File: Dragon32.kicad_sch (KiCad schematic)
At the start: 7 parts, among them IC14 74LS86AN, IC22 74LS00N, IC23 74ALS74N, IC25 LM393P, IC28 74LS393N, IC31 74LS02N

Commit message: repack layout
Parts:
- added JP4: 5vPower, Connector_PinHeader_2.54mm:PinHeader_1x02_P2.54mm_Vertical, symbol Connector:Conn_01x02_Pin
- added PL8: EDAC 392-040-558-201, Connector_PinHeader_2.54mm:PinHeader_2x20_P2.54mm_Vertical, symbol Connector_Generic:Conn_01x40
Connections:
- net +12V: now also PL8.1 (Pin_1), PL8.2 (Pin_2)
- net +5V: now also JP4.1 (Pin_1), PL8.9 (Pin_9)
- net A0: now also PL8.19 (Pin_19)
- net A1: now also PL8.20 (Pin_20)
- net A10: now also PL8.29 (Pin_29)
- net A11: now also PL8.30 (Pin_30)
- net A12: now also PL8.31 (Pin_31)
- net A13: now also PL8.37 (Pin_37)
- net A14: now also PL8.38 (Pin_38)
- net A15: now also PL8.39 (Pin_39)
- net A2: now also PL8.21 (Pin_21)
- net A3: now also PL8.22 (Pin_22)
- net A4: now also PL8.23 (Pin_23)
- net A5: now also PL8.24 (Pin_24)
- net A6: now also PL8.25 (Pin_25)
- net A7: now also PL8.26 (Pin_26)
- net A8: now also PL8.27 (Pin_27)
- net A9: now also PL8.28 (Pin_28)
- net CART: now also PL8.8 (Pin_8)
- net D0: now also PL8.10 (Pin_10)
- net D1: now also PL8.11 (Pin_11)
- net D2: now also PL8.12 (Pin_12)
- net D3: now also PL8.13 (Pin_13)
- net D4: now also PL8.14 (Pin_14)
- net D5: now also PL8.15 (Pin_15)
- net D6: now also PL8.16 (Pin_16)
- net D7: now also PL8.17 (Pin_17)
- net E: now also PL8.6 (Pin_6)
- net ESND: now also PL8.35 (Pin_35)
- net EXTMEN: now also PL8.40 (Pin_40)
- net GND: now also JP4.2 (Pin_2), PL8.33 (Pin_33), PL8.34 (Pin_34)
- net P2: now also PL8.36 (Pin_36)
- net Q: now also PL8.7 (Pin_7)
- net R2: now also PL8.32 (Pin_32)
- net R/~{W}: now also PL8.18 (Pin_18)
- net ~{HALT}: now also PL8.3 (Pin_3)
- net ~{NMI}: now also PL8.4 (Pin_4)
- net ~{RES}: now also PL8.5 (Pin_5)

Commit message: remove video
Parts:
- removed IC14: 74LS86AN, Package_DIP:DIP-14_W7.62mm, symbol 74xx:74LS86
- removed IC22: 74LS00N, Package_DIP:DIP-14_W7.62mm, symbol 74xx:74LS00
- removed IC23: 74ALS74N, Package_DIP:DIP-14_W7.62mm, symbol 74xx:74LS74
- removed IC28: 74LS393N, Package_DIP:DIP-14_W7.62mm, symbol 74xx:74LS393
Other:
- removed sheet VDG

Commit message: reinforce power rails
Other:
- added sheet Audio (audio.kicad_sch)
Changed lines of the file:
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@@
+    )
+  )
+  (sheet (at 266.7 210.82) (size 26.67 17.78) (fields_autoplaced)
+    (stroke (width 0.1524) (type solid))
+    (fill (color 0 0 0 0.0000))
+    (property "Sheetname" "Audio" (at 266.7 210.1084 0)
+      (effects (font (size 1.27 1.27)) (justify left bottom))
+    )
+    (property "Sheetfile" "audio.kicad_sch" (at 266.7 229.1846 0)
+      (effects (font (size 1.27 1.27)) (justify left top))
+    )
+    (instances
+      (project "Dragon32"
+        (path "/0c3dceba-7c95-4b3d-b590-0eb581444beb" (page "8"))
+      )
     )
   )

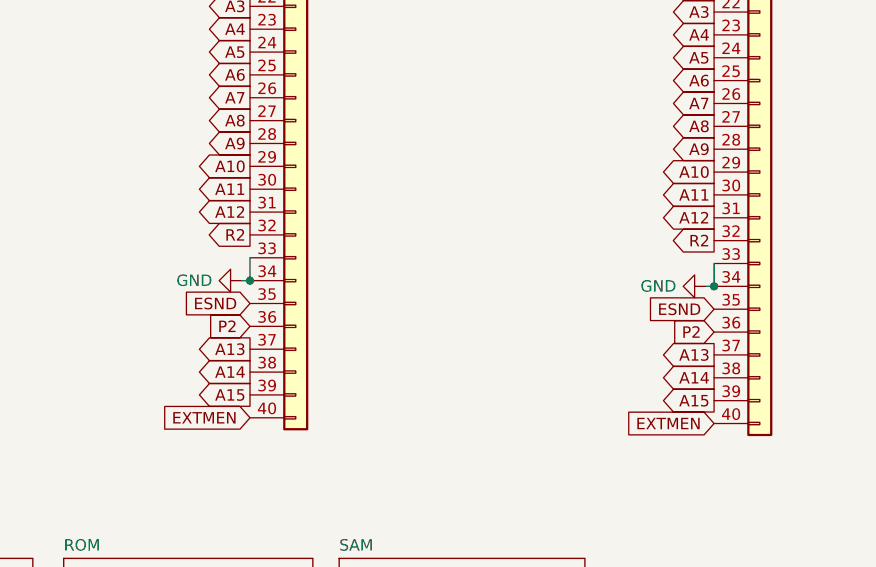
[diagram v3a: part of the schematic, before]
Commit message: reinforce audio traces
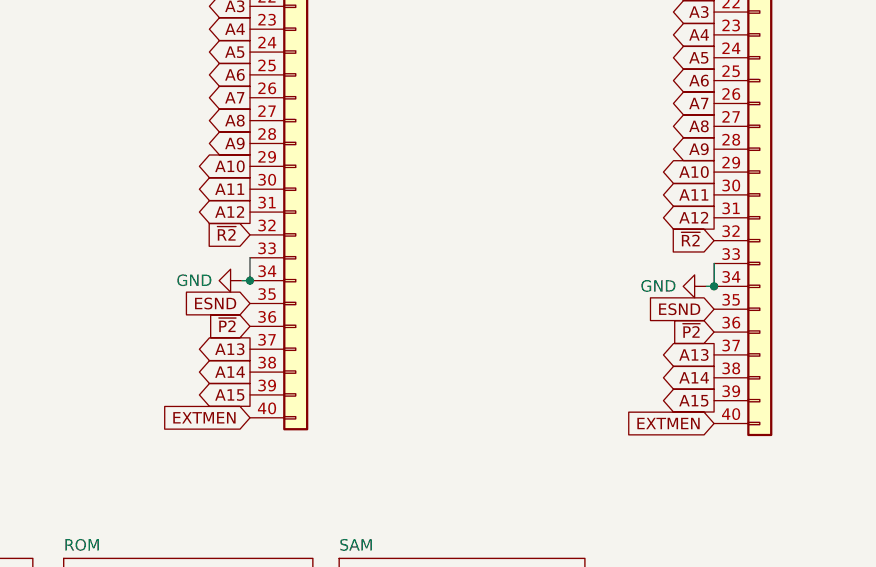
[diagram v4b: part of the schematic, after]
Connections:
- net P2 renamed ~{P2}
- net R2 renamed ~{R2}
